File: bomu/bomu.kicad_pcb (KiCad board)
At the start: 6 copper layers, 13 x 9.4 mm, 37 parts, among them U1 NRF52840-CKAA-R7

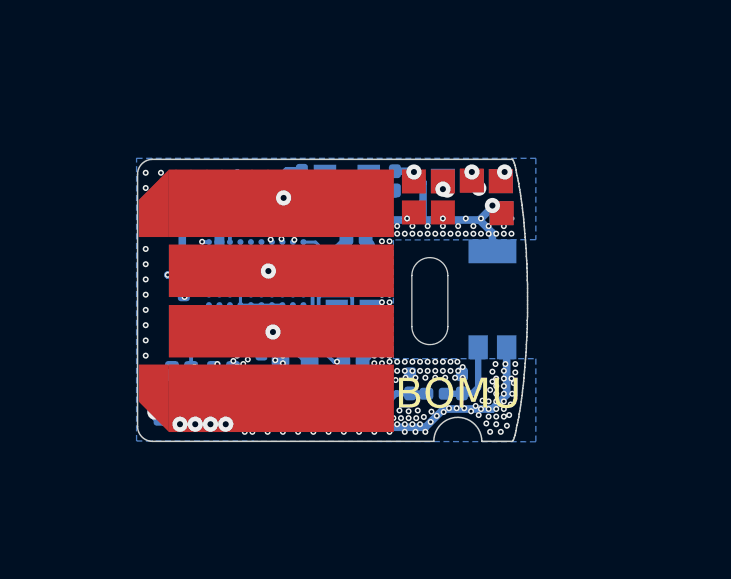
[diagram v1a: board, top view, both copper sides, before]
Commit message: Current work on BOMU 1.0.1, which address two known design defects in 1.0.0
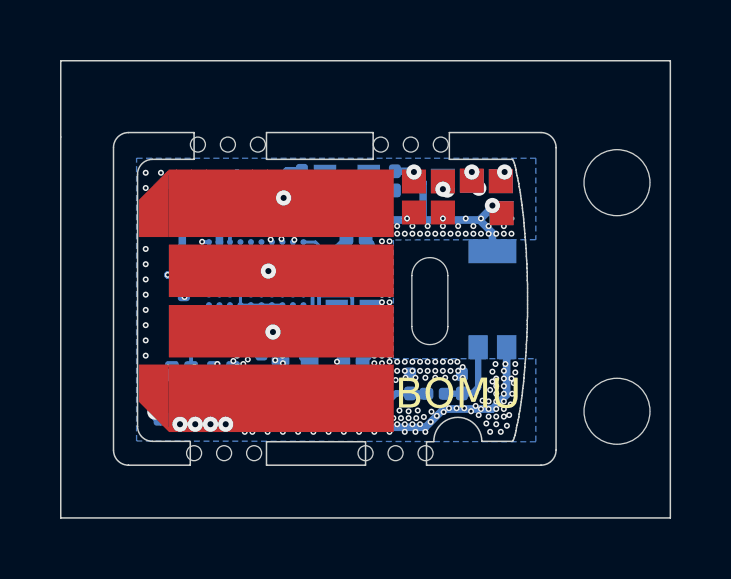
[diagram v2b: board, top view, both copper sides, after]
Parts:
- added REF**: mouse_bites, mouse_bites:mouse_bites, F.Cu at (133.9, 141.9)
- added REF**: MountingHole_2.2mm_M2, MountingHole:MountingHole_2.2mm_M2, F.Cu at (148.0, 132.9)
- added REF**: mouse_bites, mouse_bites:mouse_bites, F.Cu at (140.2, 131.6)
- added REF**: mouse_bites, mouse_bites:mouse_bites, F.Cu at (139.7, 141.9)
- added REF**: MountingHole_2.2mm_M2, MountingHole:MountingHole_2.2mm_M2, F.Cu at (148.0, 140.5)
- added REF**: mouse_bites, mouse_bites:mouse_bites, F.Cu at (134.1, 131.6)
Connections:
- U1 pad A3: Net-(U1-PadA3) -> unconnected-(U1-PadA3)
- U1 pad A4: Net-(U1-PadA4) -> unconnected-(U1-PadA4)
- U1 pad A5: Net-(U1-PadA5) -> unconnected-(U1-PadA5)
- U1 pad A6: Net-(U1-PadA6) -> unconnected-(U1-PadA6)
- U1 pad A7: Net-(U1-PadA7) -> unconnected-(U1-PadA7)
- U1 pad A9: Net-(U1-PadA9) -> unconnected-(U1-PadA9)
- U1 pad B4: Net-(U1-PadB4) -> unconnected-(U1-PadB4)
- U1 pad B5: Net-(U1-PadB5) -> unconnected-(U1-PadB5)
- U1 pad B6: Net-(U1-PadB6) -> unconnected-(U1-PadB6)
- U1 pad C5: Net-(U1-PadC5) -> unconnected-(U1-PadC5)
- U1 pad C6: Net-(U1-PadC6) -> unconnected-(U1-PadC6)
- U1 pad C7: Net-(U1-PadC7) -> unconnected-(U1-PadC7)
- U1 pad C8: Net-(U1-PadC8) -> unconnected-(U1-PadC8)
- U1 pad C9: Net-(U1-PadC9) -> unconnected-(U1-PadC9)
- U1 pad D9: Net-(U1-PadD9) -> unconnected-(U1-PadD9)
- U1 pad E10: Net-(U1-PadE10) -> unconnected-(U1-PadE10)
- U1 pad E3: Net-(U1-PadE3) -> unconnected-(U1-PadE3)
- U1 pad E9: Net-(U1-PadE9) -> unconnected-(U1-PadE9)
- U1 pad F10: Net-(U1-PadF10) -> unconnected-(U1-PadF10)
- U1 pad F3: Net-(U1-PadF3) -> unconnected-(U1-PadF3)
- U1 pad F9: Net-(U1-PadF9) -> unconnected-(U1-PadF9)
- U1 pad G1: Net-(U1-PadG1) -> unconnected-(U1-PadG1)
- U1 pad G10: Net-(U1-PadG10) -> unconnected-(U1-PadG10)
- U1 pad G2: Net-(U1-PadG2) -> unconnected-(U1-PadG2)
- U1 pad G3: Net-(U1-PadG3) -> unconnected-(U1-PadG3)
- U1 pad G9: Net-(U1-PadG9) -> unconnected-(U1-PadG9)
- U1 pad H1: Net-(U1-PadH1) -> unconnected-(U1-PadH1)
- U1 pad H4: Net-(U1-PadH4) -> unconnected-(U1-PadH4)
- U1 pad H5: Net-(U1-PadH5) -> unconnected-(U1-PadH5)
- U1 pad H6: Net-(U1-PadH6) -> unconnected-(U1-PadH6)
- U1 pad H7: Net-(U1-PadH7) -> unconnected-(U1-PadH7)
- U1 pad H8: Net-(U1-PadH8) -> unconnected-(U1-PadH8)
- U1 pad H9: Net-(U1-PadH9) -> unconnected-(U1-PadH9)
- U1 pad J1: Net-(U1-PadJ1) -> unconnected-(U1-PadJ1)
- U1 pad J3: Net-(U1-PadJ3) -> unconnected-(U1-PadJ3)
- U1 pad J4: Net-(U1-PadJ4) -> unconnected-(U1-PadJ4)
- U1 pad J5: Net-(U1-PadJ5) -> unconnected-(U1-PadJ5)
- U1 pad J6: Net-(U1-PadJ6) -> unconnected-(U1-PadJ6)
- U1 pad J7: Net-(U1-PadJ7) -> unconnected-(U1-PadJ7)
- U1 pad K2: Net-(U1-PadK2) -> unconnected-(U1-PadK2)
- U1 pad K3: Net-(U1-PadK3) -> unconnected-(U1-PadK3)
- U1 pad K4: Net-(U1-PadK4) -> unconnected-(U1-PadK4)
- U1 pad K7: Net-(U1-PadK7) -> unconnected-(U1-PadK7)
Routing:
- net GND: track 61.7 -> 63.2 mm, vias 325 -> 324
- net /NFC-: track 8.39 -> 7.83 mm
- net +3V0: track 29.4 -> 29.6 mm, vias 7 -> 8
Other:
- board size 13 x 9.4 mm -> 20.3 x 15.2 mm
- board text added: "1.0.1"
- board text removed: "1.0.0"
